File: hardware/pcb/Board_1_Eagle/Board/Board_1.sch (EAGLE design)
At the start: 88 parts, among them IC1 MCP73831, IC2 LT1963EST-1.5, IC3 VUB300, IC4 TS3A27, IC5 WTV020SD-20S, J3 DEBUG_CONNECTOR, SW1 SW_TACT_SMD, SW2 SW_TACT_SMD, SW3 SW_TACT_SMD, SW4 SW_TACT_SMD, SW5 SW_TACT_SMD, SW6 SW_TACT_SMD, SW7 SW_TACT_SMD, X1 1751248, X2 1751248, X3 1751248, Y1 CRYSTAL.3.2X2.5MM

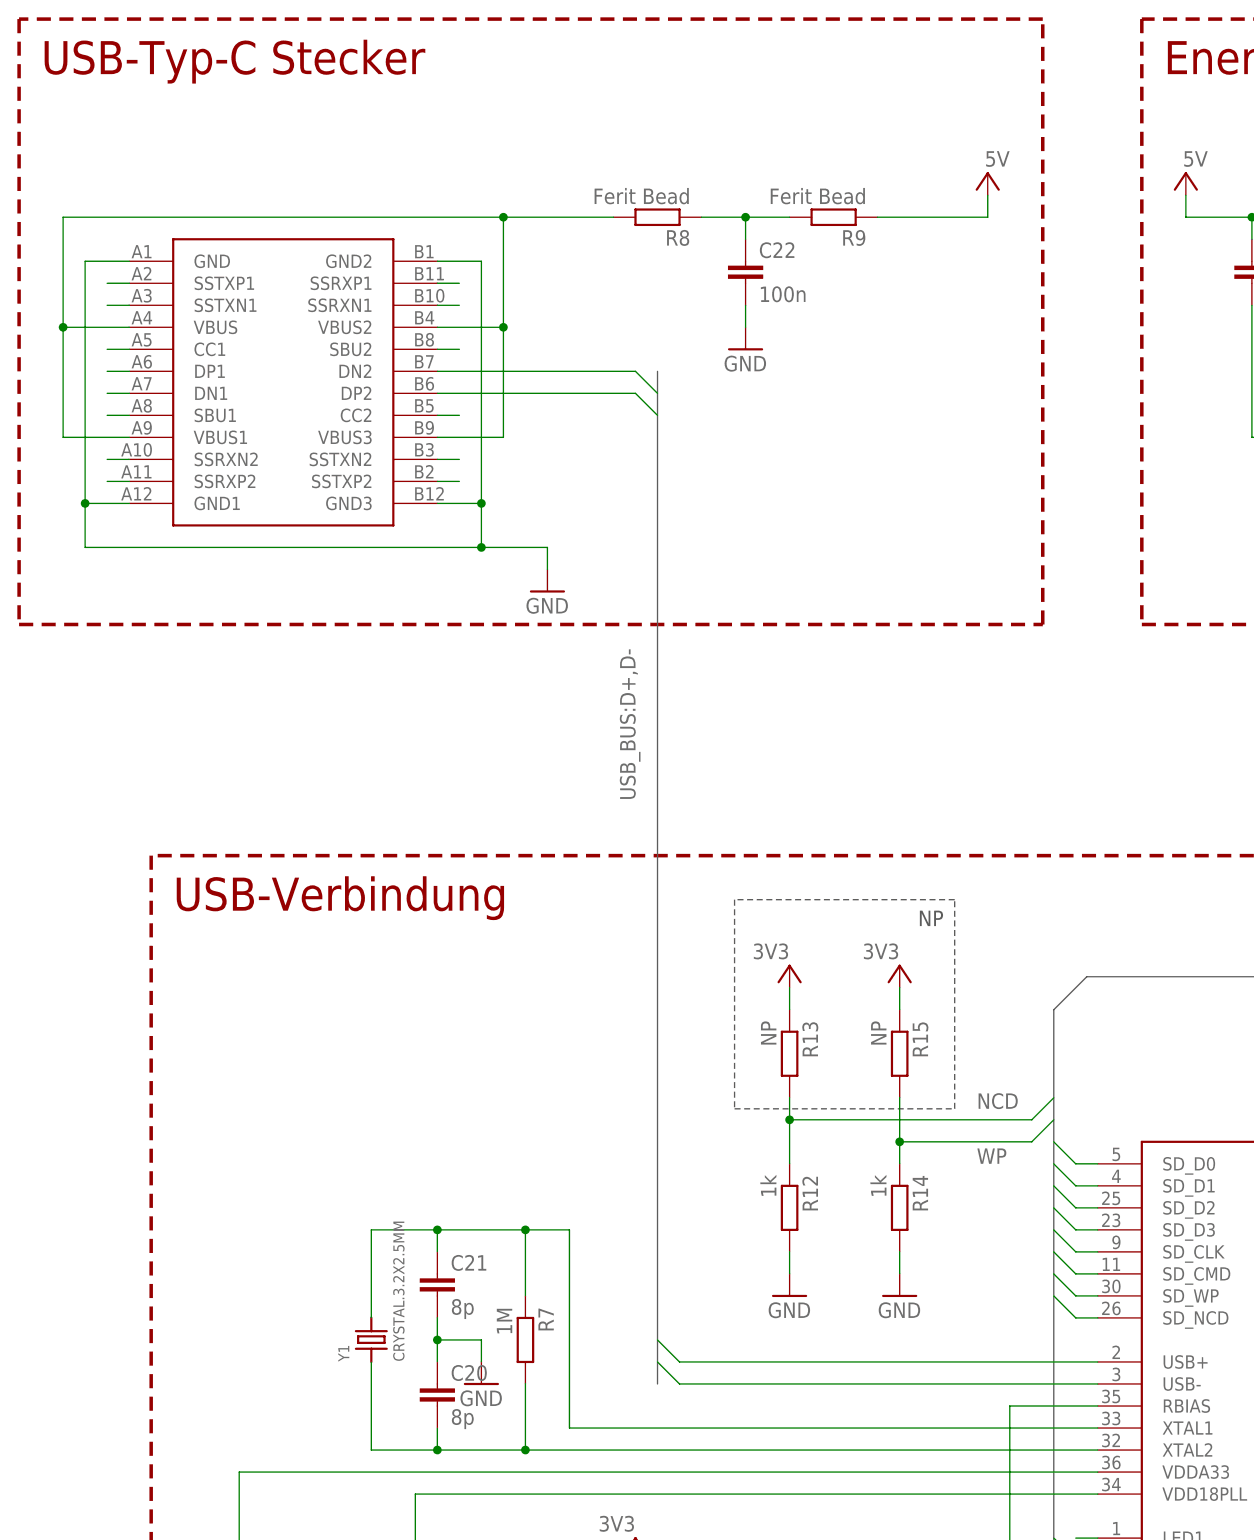
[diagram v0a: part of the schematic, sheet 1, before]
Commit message: First part of layout done and added design rules.
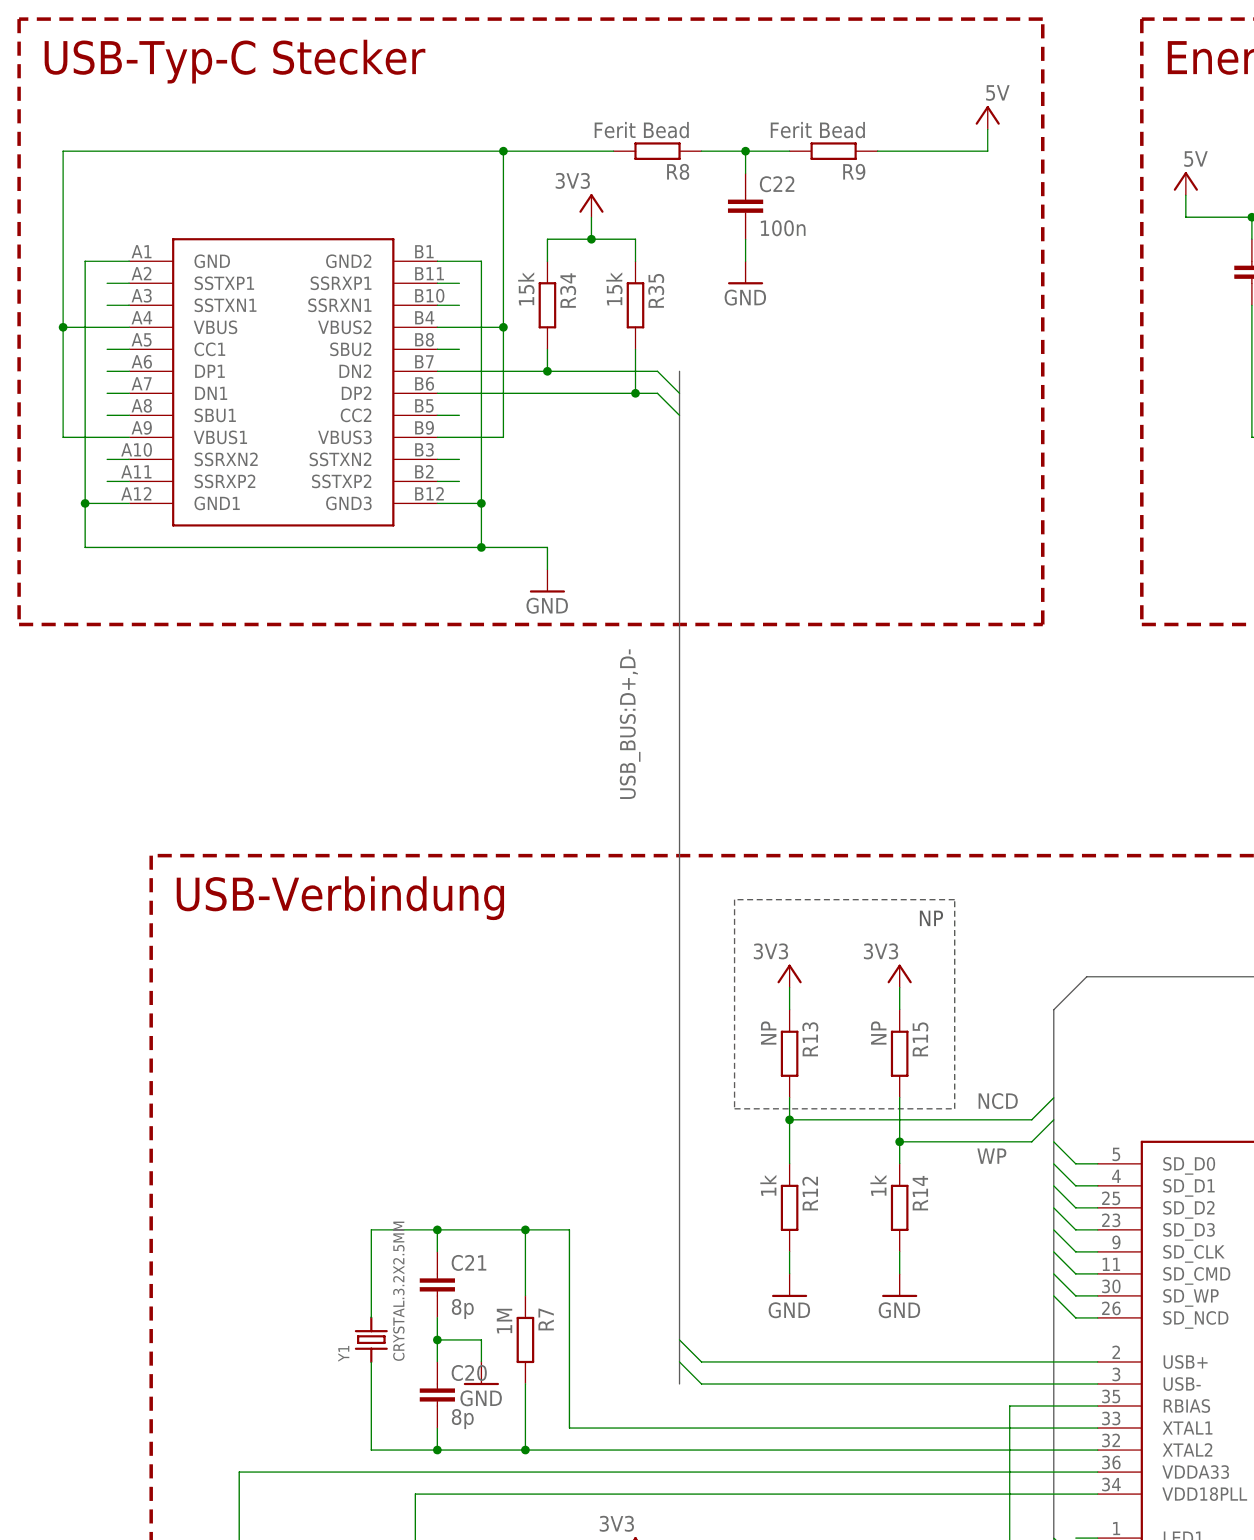
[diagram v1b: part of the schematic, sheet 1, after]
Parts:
- added R34, R35: 15k, resistor:R-EU_R0402
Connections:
- removed net N$51: R31.2
- net +3V3: now also R34.1, R35.1
- net D+: now also R35.2
- net D-: now also R34.2
- net V+: now also R31.2
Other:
- moved on the sheet: C22, R8, R9

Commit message: VUB300 gelayoutet
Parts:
- C10, C11, C12, C13, C14, C15, C16, C17, C18, C19, C20, C21, C7, C8, C9: device rcl:C-EUC0603 -> rcl:C-EUC0402
- R12, R13, R14, R15, R4, R5, R6, R7: device resistor:R-EU_R0603 -> resistor:R-EU_R0402
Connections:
- net D+ renamed D_P
- net D- renamed D_N
